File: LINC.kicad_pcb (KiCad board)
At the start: 4 copper layers, 55.1 x 58 mm, 39 parts, among them J1 112-024-113R001, J2 FTSH-105-01-L-DV-K, J3 RJHSE5380, J4 USB4085-GF-A, U1 SN74LVC8T245PWR, U2 SN74LVC07APWR, U3 STM32H523RETx, U4 TLV74311PDBVR, U5 THVD1451D, U6 SN74LVC1G07DCKR, U7 SN74LVC14APWR, U8 USBLC6-2SC6, Y1 MU00525-32.768K, Y2 CS10820-24M

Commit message: Update resistor pack
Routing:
- net /Overview/Microcontroller/CTRL_RX: track 36.3 -> 23.9 mm
- net /Overview/Microcontroller/CTRL_TX: track 36.1 -> 24.1 mm
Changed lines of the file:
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@@
 		(tags "SOIC SO")
 		(property "Reference" "U5"
-			(at -4.29 -1.3075 0)
+			(at -4.07 1.97 0)
 			(layer "F.SilkS")
 			(effects
 				(font
-					(size 1 1)
-					(thickness 0.15)
+					(size 0.5 0.5)
+					(thickness 0.075)
 				)
 			)
@@
 			)
 		)
-		(property "Datasheet" "https://industrial.panasonic.com/cdbs/www-data/pdf/AOC0000/AOC0000C14.pdf"
+		(property "Datasheet" "https://yageogroup.com/content/Resource%20Library/Datasheet/PYU-YC_TC_GROUP_51_ROHS_L.pdf"
 			(at 0 0 270)
 			(unlocked yes)
@@
 			)
 		)
-		(property "Description" "2.2k Ohm ±5% 62.5mW Power Per Element Isolated 8 Resistor Network/Array ±200ppm/°C 1506, Convex, Long Side Terminals"
+		(property "Description" "2.2k Ohm ±5% 62.5mW Power Per Element Isolated 8 Resistor Network/Array ±200ppm/°C 1606, Convex, Long Side Terminals"
 			(at 0 0 270)
 			(unlocked yes)
@@
 			)
 		)
-		(property "Part-DB URL" "http://parts.husbylabs.com/en/part/29/info"
+		(property "Part-DB URL" "http://parts.husbylabs.com/en/part/33/info"
 			(at 0 0 270)
 			(unlocked yes)
@@
 			)
 		)
-		(property "Manufacturer" "Panasonic Electronic Components"
+		(property "Manufacturer" "YAGEO"
 			(at 0 0 270)
 			(unlocked yes)
@@
 			)
 		)
-		(property "MPN" "EXB-2HV222JV"
+		(property "MPN" "YC248-JR-072K2L"
 			(at 0 0 270)
 			(unlocked yes)
@@
 			)
 		)
-		(property "Part-DB ID" "29"
+		(property "Part-DB ID" "33"
 			(at 0 0 270)
 			(unlocked yes)
@@
 			)
 		)
-		(property "manf" "Panasonic Electronic Components"
+		(property "manf" "YAGEO"
 			(at 0 0 270)
 			(unlocked yes)
@@
 			)
 		)
-		(property "manf#" "EXB-2HV222JV"
+		(property "manf#" "YC248-JR-072K2L"
 			(at 0 0 270)
 			(unlocked yes)
@@
 			)
 		)
-		(property "DigiKey SPN" "Y1222DKR-ND"
+		(property "DigiKey SPN" "13-YC248-JR-072K2LCT-ND"
 			(at 0 0 270)
 			(unlocked yes)
@@
 			)
 		)
-		(property "digikey#" "Y1222DKR-ND"
+		(property "digikey#" "13-YC248-JR-072K2LCT-ND"
 			(at 0 0 270)
 			(unlocked yes)
@@
 			)
 		)
+		(property "Part-DB Footprint" "-"
+			(at 0 0 270)
+			(unlocked yes)
+			(layer "F.Fab")
+			(hide yes)
+			(effects
+				(font
+					(size 1 1)
+					(thickness 0.15)
+				)
+			)
+		)
 		(property ki_fp_filters "Resistor_SMD:R_Array_Convex_8x0602")
 		(sheetname "/Overview/GPIB Transceiver/")
@@
 	)
 	(segment
+		(start 169.090501 104.843898)
+		(end 173.583001 104.843898)
+		(width 0.2)
+		(layer "F.Cu")
+		(net "Net-(D2-K)")
+	)
+	(segment
+		(start 173.583001 104.843898)
+		(end 173.585501 104.846398)
+		(width 0.2)
+		(layer "F.Cu")
+		(net "Net-(D2-K)")
+	)
+	(segment
+		(start 169.090501 101.566399)
+		(end 169.090501 103.268898)
+		(width 0.2)
+		(layer "F.Cu")
+		(net "Net-(D2-A)")
+	)
+	(segment
+		(start 167.665501 100.916398)
+		(end 168.4405 100.916398)
+		(width 0.2)
+		(layer "F.Cu")
+		(net "Net-(D2-A)")
+	)
+	(segment
+		(start 168.4405 100.916398)
+		(end 169.090501 101.566399)
+		(width 0.2)
+		(layer "F.Cu")
+		(net "Net-(D2-A)")
+	)
+	(segment
 		(start 167.615501 101.366398)
 		(end 167.665501 101.416398)
@@
 	)
 	(segment
-		(start 139.790501 96.066398)
-		(end 140.190501 96.466398)
-		(width 0.2)
-		(layer "F.Cu")
-		(net "/Overview/Microcontroller/CTRL_TX")
-	)
-	(segment
 		(start 157.540501 94.916398)
 		(end 157.990501 94.466398)
@@
 	)
 	(segment
-		(start 140.190501 105.705663)
-		(end 142.855501 108.370663)
+		(start 142.855501 110.191398)
+		(end 142.855501 109.161398)
 		(width 0.2)
 		(layer "F.Cu")
@@
 	)
 	(segment
-		(start 142.855501 108.370663)
-		(end 142.855501 110.191398)
+		(start 142.855501 109.161398)
+		(end 143.880501 108.136398)
 		(width 0.2)
 		(layer "F.Cu")
@@
 		(net "/Overview/Microcontroller/CTRL_TX")
 	)
-	(segment
-		(start 140.190501 96.466398)
-		(end 140.190501 105.705663)
-		(width 0.2)
-		(layer "F.Cu")
-		(net "/Overview/Microcontroller/CTRL_TX")
-	)
 	(via
 		(at 157.990501 94.466398)
@@
 	)
 	(via
-		(at 139.790501 96.066398)
+		(at 143.880501 108.136398)
 		(size 0.6)
 		(drill 0.3)
@@
 	)
 	(segment
-		(start 156.390501 96.066398)
-		(end 139.790501 96.066398)
+		(start 143.880501 108.136398)
+		(end 144.320501 108.136398)
 		(width 0.2)
 		(layer "B.Cu")
@@
 	)
 	(segment
-		(start 157.990501 94.466398)
-		(end 156.390501 96.066398)
+		(start 144.320501 108.136398)
+		(end 157.990501 94.466398)
 		(width 0.2)
 		(layer "B.Cu")
@@
 	)
 	(segment
-		(start 140.490501 96.866398)
-		(end 140.490501 105.581399)
+		(start 144.125501 109.111398)
+		(end 144.860501 108.376398)
 		(width 0.2)
 		(layer "F.Cu")
@@
 	)
 	(segment
-		(start 140.690501 96.666398)
-		(end 140.490501 96.866398)
-		(width 0.2)
-		(layer "F.Cu")
-		(net "/Overview/Microcontroller/CTRL_RX")
-	)
-	(segment
-		(start 144.125501 109.216399)
-		(end 144.125501 110.191398)
+		(start 144.125501 110.191398)
+		(end 144.125501 109.111398)
 		(width 0.2)
 		(layer "F.Cu")
@@
 		(net "/Overview/Microcontroller/CTRL_RX")
 	)
-	(segment
-		(start 140.490501 105.581399)
-		(end 144.125501 109.216399)
-		(width 0.2)
-		(layer "F.Cu")
-		(net "/Overview/Microcontroller/CTRL_RX")
-	)
 	(via
 		(at 158.590501 94.866398)
@@
 	)
 	(via
-		(at 140.690501 96.666398)
+		(at 144.860501 108.376398)
 		(size 0.6)
 		(drill 0.3)
@@
 	)
 	(segment
-		(start 140.990501 96.366398)
-		(end 157.090501 96.366398)
-		(width 0.2)
-		(layer "B.Cu")
-		(net "/Overview/Microcontroller/CTRL_RX")
-	)
-	(segment
-		(start 140.690501 96.666398)
-		(end 140.990501 96.366398)
+		(start 144.860501 108.376398)
+		(end 145.080501 108.376398)
 		(width 0.2)
 		(layer "B.Cu")
@@
 	)
 	(segment
-		(start 157.090501 96.366398)
+		(start 145.080501 108.376398)
 		(end 158.590501 94.866398)
 		(width 0.2)
@@
 	)
 	(segment
-		(start 181.490501 118.866398)
-		(end 181.490501 120.387295)
-		(width 0.2)
-		(layer "F.Cu")
-		(net "Net-(D1-K)")
-	)
-	(segment
-		(start 181.490501 120.387295)
-		(end 181.501002 120.397796)
-		(width 0.2)
-		(layer "F.Cu")
-		(net "Net-(D1-K)")
-	)
-	(segment
 		(start 145.97 78.89)
 		(end 145.97 79.49)
@@
 	)
 	(segment
-		(start 169.090501 104.843898)
-		(end 173.583001 104.843898)
-		(width 0.2)
-		(layer "F.Cu")
-		(net "Net-(D2-K)")
-	)
-	(segment
-		(start 173.583001 104.843898)
-		(end 173.585501 104.846398)
-		(width 0.2)
-		(layer "F.Cu")
-		(net "Net-(D2-K)")
-	)
-	(segment
-		(start 169.090501 101.566399)
-		(end 169.090501 103.268898)
-		(width 0.2)
-		(layer "F.Cu")
-		(net "Net-(D2-A)")
-	)
-	(segment
-		(start 167.665501 100.916398)
-		(end 168.4405 100.916398)
+		(start 181.490501 118.866398)
+		(end 181.490501 120.387295)
 		(width 0.2)
 		(layer "F.Cu")
-		(net "Net-(D2-A)")
+		(net "Net-(D1-K)")
 	)
 	(segment
-		(start 168.4405 100.916398)
-		(end 169.090501 101.566399)
+		(start 181.490501 120.387295)
+		(end 181.501002 120.397796)
 		(width 0.2)
 		(layer "F.Cu")
-		(net "Net-(D2-A)")
+		(net "Net-(D1-K)")
 	)
 	(zone

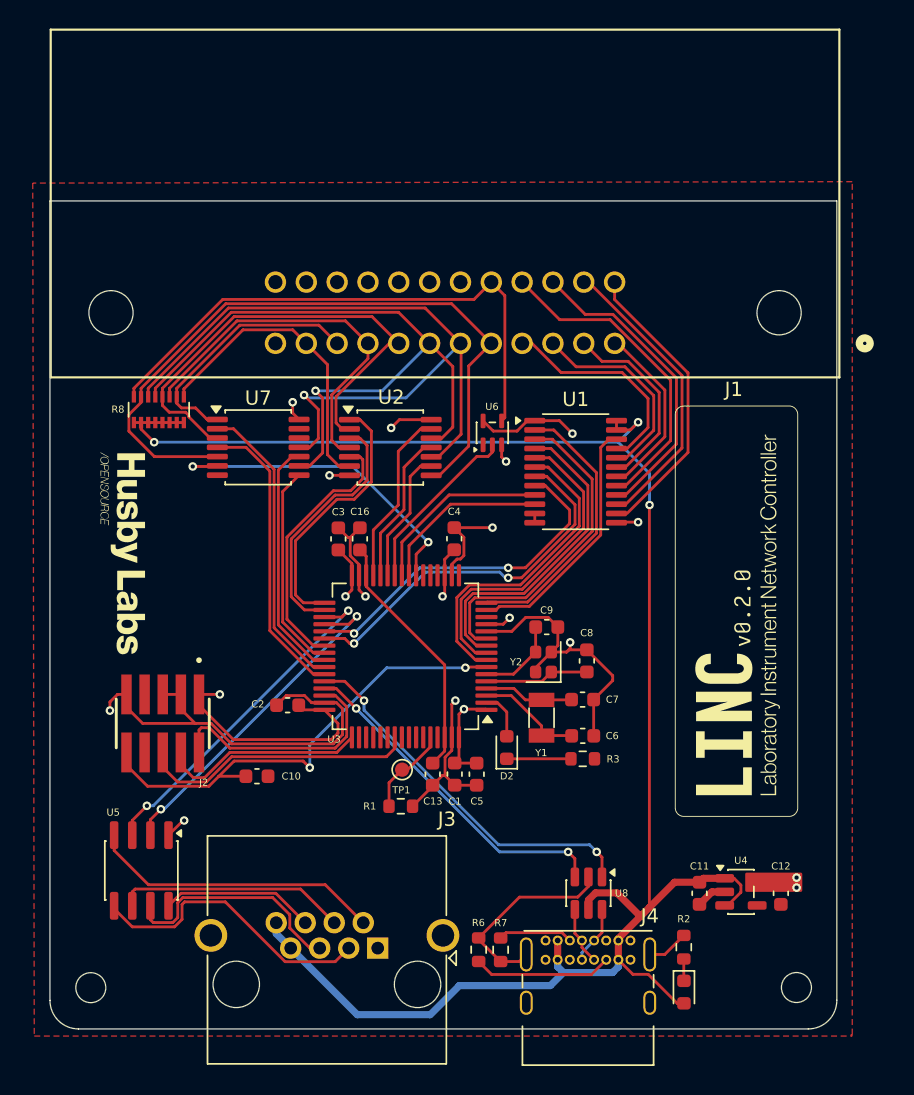
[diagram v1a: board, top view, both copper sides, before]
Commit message: Add ground plane to bottom layer
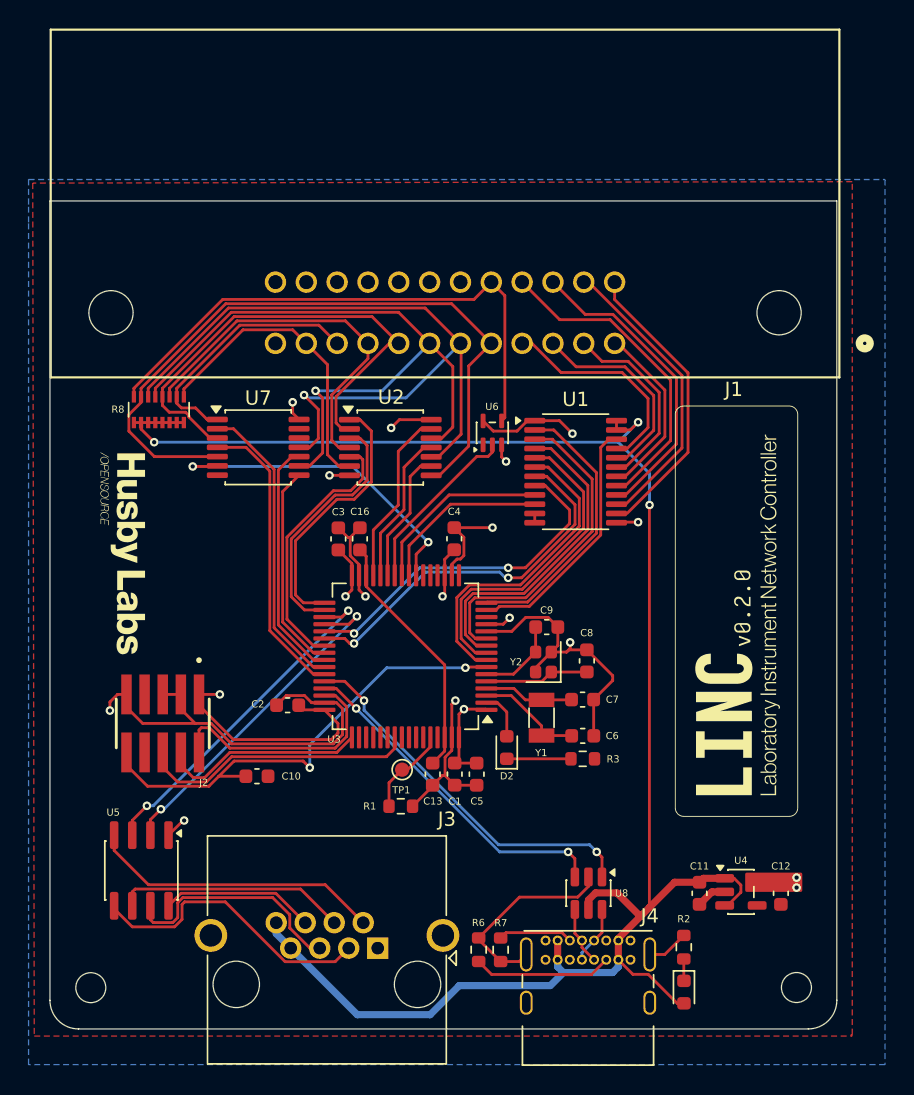
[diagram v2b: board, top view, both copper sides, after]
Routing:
- added copper zone on B.Cu, net GND
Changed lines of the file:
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@@
+	)
+	(zone
+		(net "GND")
+		(layer "B.Cu")
+		(hatch edge 0.5)
+		(priority 3)
+		(connect_pads
+			(clearance 0.5)
+		)
+		(min_thickness 0.25)
+		(fill yes
+			(thermal_gap 0.5)
+			(thermal_bridge_width 0.5)
+			(island_removal_mode 0)
+		)
+		(polygon
+			(pts
+				(xy 135.590502 64.266398) (xy 195.590502 64.266398) (xy 195.590502 126.266398) (xy 135.590502 126.266398)
+				(xy 135.590502 67.266397) (xy 135.590501 66.016398) (xy 135.590501 64.266399)
+			)
+		)
 	)
 	(zone
@@
 		(polygon
 			(pts
-				(xy 192.220501 123.876398) (xy 192.311977 65.209467) (xy 136.974716 65.123181) (xy 136.900501 123.816398)
+				(xy 194.284765 123.878637) (xy 194.376239 65.212686) (xy 133.527612 65.117806) (xy 133.453394 123.812659)
 			)
 		)
@@
 		(polygon
 			(pts
-				(xy 193.590502 64.366398) (xy 193.590502 133.25) (xy 133.5 133.25) (xy 133.5 64.366398)
+				(xy 193.590502 64.366398) (xy 193.590502 124.906398) (xy 135.280502 124.906398) (xy 135.280502 64.366398)
 			)
 		)

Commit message: BOM Reduction
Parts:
- R1: value 10k -> 1k
- U4: value TLV74311PDBVR -> TLV74333PDBVR
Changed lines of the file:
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@@
 			)
 		)
-		(property "Value" "TLV74311PDBVR"
+		(property "Value" "TLV74333PDBVR"
 			(at 0 2.4 0)
 			(layer "F.Fab")
@@
 			)
 		)
-		(property "Part-DB URL" "http://parts.husbylabs.com/en/part/31/info"
+		(property "Part-DB URL" "http://parts.husbylabs.com/en/part/34/info"
 			(at 0 0 0)
 			(unlocked yes)
@@
 			)
 		)
-		(property "MPN" "TLV74311PDBVR"
+		(property "MPN" "TLV74333PDBVR"
 			(at 0 0 0)
 			(unlocked yes)
@@
 			)
 		)
-		(property "Part-DB ID" "31"
+		(property "Part-DB ID" "34"
 			(at 0 0 0)
 			(unlocked yes)
@@
 			)
 		)
-		(property "manf#" "TLV74311PDBVR"
+		(property "manf#" "TLV74333PDBVR"
 			(at 0 0 0)
 			(unlocked yes)
@@
 			)
 		)
-		(property "DigiKey SPN" "296-50002-6-ND"
+		(property "DigiKey SPN" "296-47852-6-ND"
 			(at 0 0 0)
 			(unlocked yes)
@@
 			)
 		)
-		(property "digikey#" "296-50002-6-ND"
+		(property "digikey#" "296-47852-6-ND"
 			(at 0 0 0)
 			(unlocked yes)
@@
 			)
 		)
-		(property "Value" "10k"
+		(property "Value" "1k"
 			(at 0 1.43 0)
 			(layer "F.Fab")
@@
 			)
 		)
-		(property "Description" "10 kOhms ±1% 0.1W, 1/10W Chip Resistor 0603 (1608 Metric) Moisture Resistant Thick Film"
+		(property "Description" "1 kOhms ±1% 0.1W, 1/10W Chip Resistor 0603 (1608 Metric) Moisture Resistant Thick Film"
 			(at 0 0 0)
 			(layer "F.Fab")
@@
 			)
 		)
-		(property "Part-DB URL" "http://parts.husbylabs.com/en/part/10/info"
+		(property "Part-DB URL" "http://parts.husbylabs.com/en/part/32/info"
 			(at 0 0 0)
 			(unlocked yes)
@@
 			)
 		)
-		(property "MPN" "RC0603FR-0710KL"
+		(property "MPN" "RC0603FR-071KL"
 			(at 0 0 0)
 			(unlocked yes)
@@
 			)
 		)
-		(property "Part-DB ID" "10"
+		(property "Part-DB ID" "32"
 			(at 0 0 0)
 			(unlocked yes)
@@
 			)
 		)
-		(property "manf#" "RC0603FR-0710KL"
+		(property "manf#" "RC0603FR-071KL"
 			(at 0 0 0)
 			(unlocked yes)
@@
 			)
 		)
-		(property "DigiKey SPN" "311-10.0KHRDKR-ND"
+		(property "DigiKey SPN" "311-1.00KHRDKR-ND"
 			(at 0 0 0)
 			(unlocked yes)
@@
 			)
 		)
-		(property "digikey#" "311-10.0KHRDKR-ND"
+		(property "digikey#" "311-1.00KHRDKR-ND"
 			(at 0 0 0)
 			(unlocked yes)

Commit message: Final v0.2.0
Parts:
- D1: value Green -> Red
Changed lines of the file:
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@@
 			)
 		)
-		(property "Value" "Green"
+		(property "Value" "Red"
 			(at 0 1.43 90)
 			(layer "F.Fab")
@@
 			)
 		)
-		(property "Datasheet" "https://optoelectronics.liteon.com/upload/download/DS22-2000-228/LTST-C191KGKT.PDF"
+		(property "Datasheet" "https://optoelectronics.liteon.com/upload/download/DS22-2000-223/LTST-C191KRKT.PDF"
 			(at 0 0 90)
 			(layer "F.Fab")
@@
 			)
 		)
-		(property "Description" "Green 571nm LED Indication - Discrete 2V 0603 (1608 Metric)"
+		(property "Description" "Red 631nm LED Indication - Discrete 2V 0603 (1608 Metric)"
 			(at 0 0 90)
 			(layer "F.Fab")
@@
 			)
 		)
-		(property "Part-DB URL" "http://parts.husbylabs.com/en/part/21/info"
+		(property "Part-DB URL" "http://parts.husbylabs.com/en/part/22/info"
 			(at 0 0 270)
 			(unlocked yes)
@@
 			)
 		)
-		(property "MPN" "LTST-C191KGKT"
+		(property "MPN" "LTST-C191KRKT"
 			(at 0 0 270)
 			(unlocked yes)
@@
 			)
 		)
-		(property "Part-DB ID" "21"
+		(property "Part-DB ID" "22"
 			(at 0 0 270)
 			(unlocked yes)
@@
 			)
 		)
-		(property "manf#" "LTST-C191KGKT"
+		(property "manf#" "LTST-C191KRKT"
 			(at 0 0 270)
 			(unlocked yes)
@@
 			)
 		)
-		(property "DigiKey SPN" "160-1446-6-ND"
+		(property "DigiKey SPN" "160-1447-6-ND"
 			(at 0 0 270)
 			(unlocked yes)
@@
 			)
 		)
-		(property "digikey#" "160-1446-6-ND"
+		(property "digikey#" "160-1447-6-ND"
 			(at 0 0 270)
 			(unlocked yes)
